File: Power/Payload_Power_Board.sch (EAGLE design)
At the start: 58 parts, among them J0_PLOAD_CONN 0039281023, J1_BBB 105313-1102, J2_LORA 105313-1102, J3_SPOT 105313-1102, J4_SSSONAR 43650-0218, Q1 FQD11P06TM

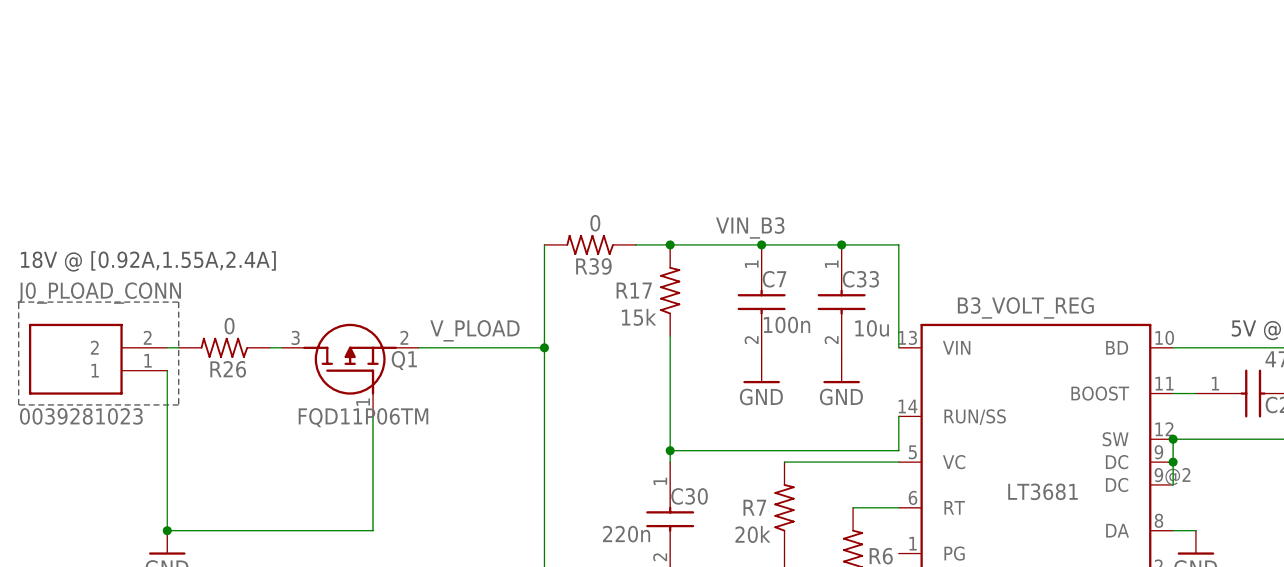
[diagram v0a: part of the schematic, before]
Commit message: Updated the expected input voltage range
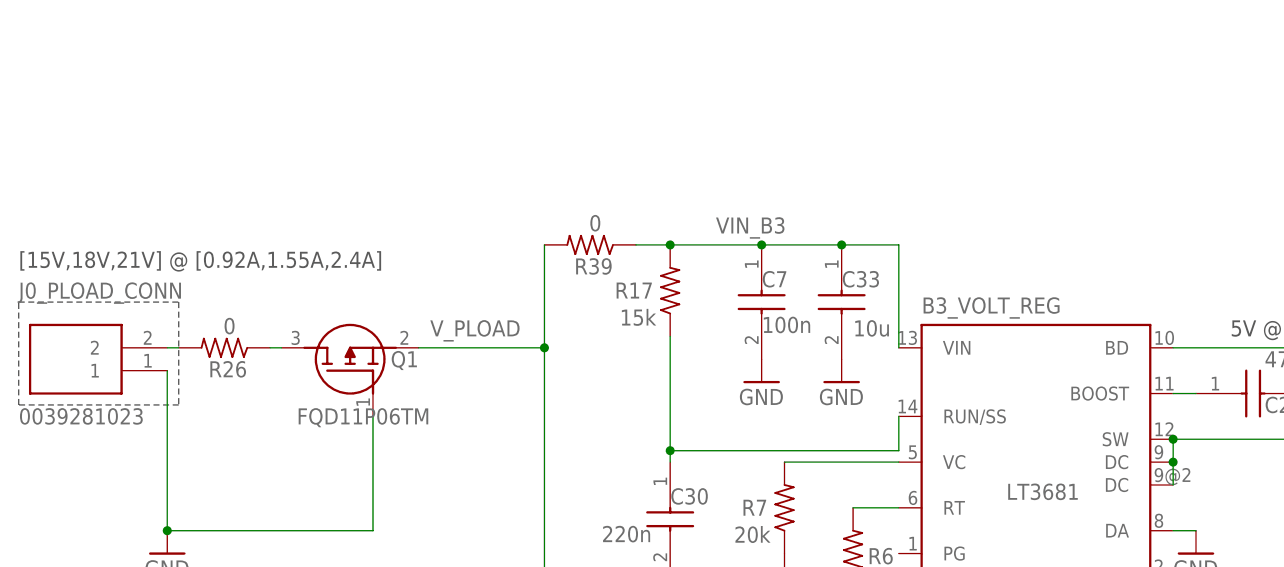
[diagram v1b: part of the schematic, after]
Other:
- note added: "[15V,18V,21V] @ [0.92A,1.55A,2.4A]"
- note removed: "18V @ [0.92A,1.55A,2.4A]"
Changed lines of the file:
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@@
 <setting verticaltext="up"/>
 </settings>
-<grid distance="50" unitdist="mil" unit="mil" style="lines" multiple="2" display="yes" altdistance="0.01" altunitdist="inch" altunit="mil"/>
+<grid distance="0.1" unitdist="inch" unit="inch" style="lines" multiple="1" display="no" altdistance="0.01" altunitdist="inch" altunit="inch"/>
 <layers>
 <layer number="1" name="Top" color="4" fill="1" visible="no" active="no"/>
@@
 <text x="176.53" y="118.11" size="1.778" layer="97">2x22uF and 1x6.8uF caps to be stacked vertically</text>
 <text x="176.53" y="63.5" size="1.778" layer="97">2x22uF and 1x6.8uF caps to be stacked vertically</text>
-<text x="5.08" y="203.2" size="1.778" layer="97">18V @ [0.92A,1.55A,2.4A]</text>
 <text x="208.28" y="180.34" size="1.778" layer="97">Connector "J1_BBB" powers the Payload's
 BeagleBone Black uprocessor</text>
@@
 power from the "J3 Pload" connector on the
 AUV's existing Power Controller Board</text>
+<text x="5.08" y="203.2" size="1.778" layer="97">[15V,18V,21V] @ [0.92A,1.55A,2.4A]</text>
 </plain>
 <instances>
@@
 </instance>
 <instance part="B3_VOLT_REG" gate="G$1" x="118.11" y="181.61" smashed="yes">
-<attribute name="NAME" x="109.22" y="198.12" size="1.778" layer="95"/>
+<attribute name="NAME" x="105.41" y="198.12" size="1.778" layer="95"/>
 <attribute name="VALUE" x="114.81" y="177.42" size="1.778" layer="96"/>
 </instance>
